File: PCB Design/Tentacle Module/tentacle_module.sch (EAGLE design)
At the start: 58 parts, among them IC1 5.0V, IC3 3.3V, T1 NTD5867NL, T2 NTD5867NL, T3 NTD5867NL, T4 NTD5867NL, U1 OKR-T/10-W12, X3 RJ45-8X, X4 RJ45-8X

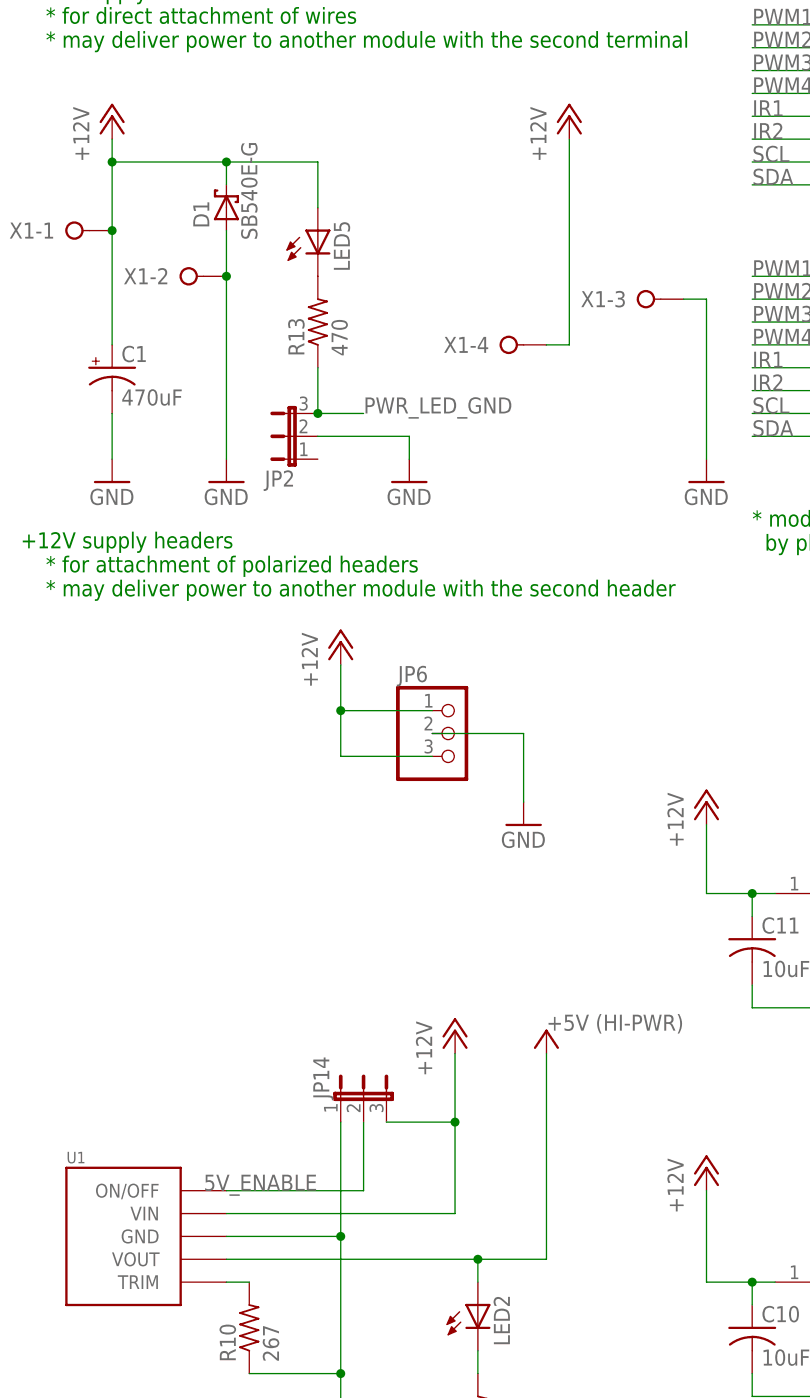
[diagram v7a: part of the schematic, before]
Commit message: Finished updating the Tentacle board
not polished yet though
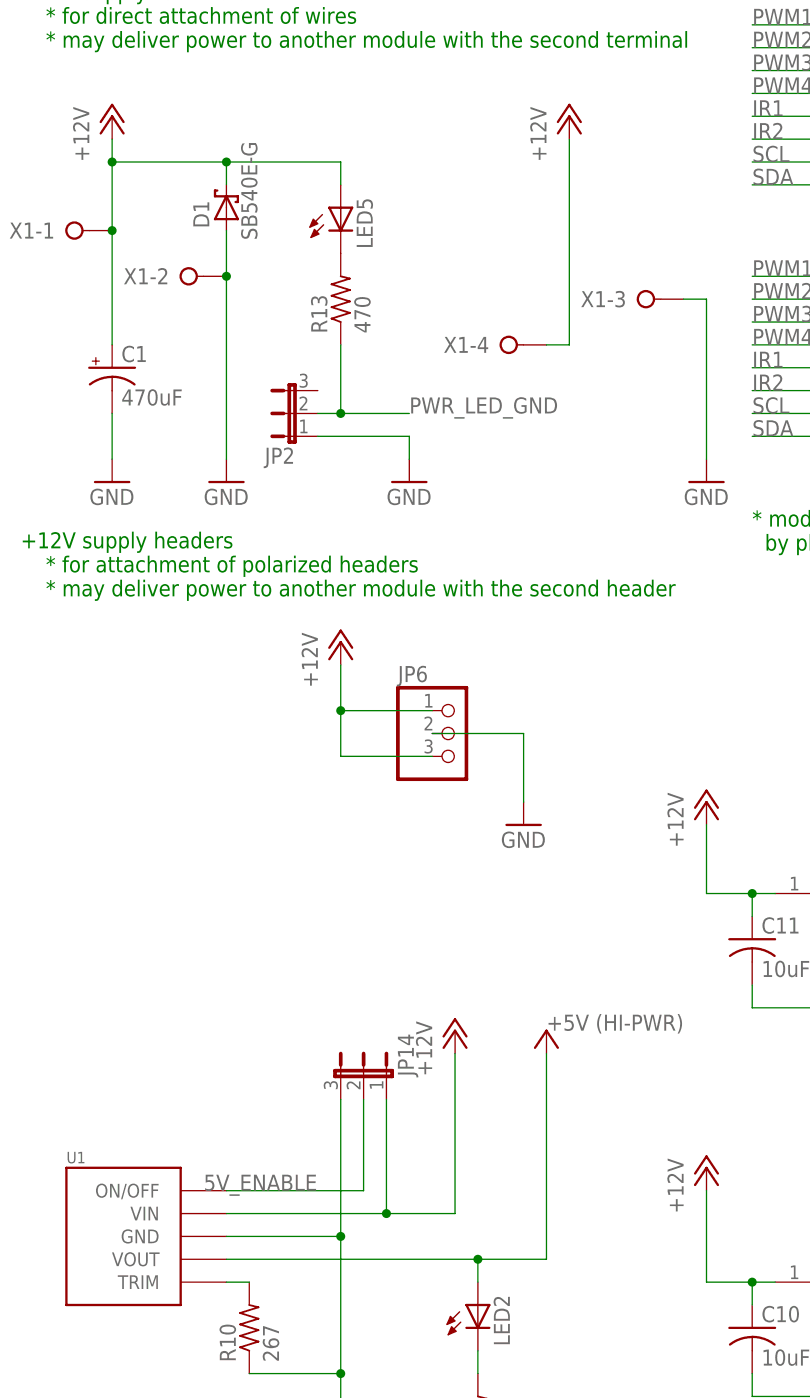
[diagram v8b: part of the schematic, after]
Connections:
- net +12V: now also JP14.1; no longer JP14.3
- net GND: now also JP14.3, JP2.1; no longer JP14.1, JP2.2
- net PWR_LED_GND: now also JP2.2; no longer JP2.3
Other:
- moved on the sheet: JP14, JP2, LED5, R13
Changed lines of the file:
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@@
 <?xml version="1.0" encoding="utf-8"?>
 <!DOCTYPE eagle SYSTEM "eagle.dtd">
-<eagle version="7.0.0">
+<eagle version="7.1.0">
 <drawing>
 <settings>
@@
 <attribute name="VALUE" x="39.751" y="175.006" size="1.778" layer="96" rot="R270"/>
 </instance>
-<instance part="LED5" gate="G$1" x="48.26" y="165.1"/>
-<instance part="R13" gate="G$1" x="48.26" y="154.94" rot="R90"/>
+<instance part="LED5" gate="G$1" x="50.8" y="167.64"/>
+<instance part="R13" gate="G$1" x="50.8" y="157.48" rot="R90"/>
 <instance part="X6" gate="-1" x="226.06" y="109.22"/>
 <instance part="X6" gate="-2" x="226.06" y="104.14"/>
@@
 <instance part="U1" gate="G$1" x="27.94" y="53.34"/>
 <instance part="P+13" gate="1" x="63.5" y="76.2"/>
-<instance part="JP14" gate="1" x="53.34" y="68.58"/>
+<instance part="JP14" gate="1" x="53.34" y="71.12" rot="MR0"/>
 <instance part="PE1" gate="1" x="50.8" y="22.86"/>
 <instance part="P+3" gate="1" x="73.66" y="76.2" smashed="yes">
@@
 <instance part="LED2" gate="G$1" x="66.04" y="45.72"/>
 <instance part="R11" gate="G$1" x="66.04" y="33.02" rot="R90"/>
-<instance part="JP2" gate="1" x="45.72" y="142.24" rot="R90"/>
+<instance part="JP2" gate="1" x="45.72" y="144.78" rot="R90"/>
 <instance part="C3" gate="G$1" x="139.7" y="86.36"/>
 <instance part="C5" gate="G$1" x="139.7" y="43.18"/>
@@
 <pinref part="D1" gate="G$1" pin="C"/>
 <wire x1="38.1" y1="172.72" x2="38.1" y2="170.18" width="0.1524" layer="91"/>
-<wire x1="38.1" y1="172.72" x2="48.26" y2="172.72" width="0.1524" layer="91"/>
+<wire x1="38.1" y1="172.72" x2="50.8" y2="172.72" width="0.1524" layer="91"/>
 <junction x="38.1" y="172.72"/>
 <pinref part="X1" gate="-1" pin="KL"/>
 <junction x="25.4" y="165.1"/>
 <pinref part="LED5" gate="G$1" pin="A"/>
-<wire x1="48.26" y1="172.72" x2="48.26" y2="167.64" width="0.1524" layer="91"/>
+<wire x1="50.8" y1="172.72" x2="50.8" y2="170.18" width="0.1524" layer="91"/>
 </segment>
 <segment>
@@
 <pinref part="U1" gate="G$1" pin="VIN"/>
 <pinref part="P+13" gate="1" pin="+12V"/>
-<wire x1="38.1" y1="55.88" x2="63.5" y2="55.88" width="0.1524" layer="91"/>
-<wire x1="63.5" y1="55.88" x2="63.5" y2="66.04" width="0.1524" layer="91"/>
-<pinref part="JP14" gate="1" pin="3"/>
-<wire x1="63.5" y1="66.04" x2="63.5" y2="73.66" width="0.1524" layer="91"/>
-<wire x1="55.88" y1="66.04" x2="63.5" y2="66.04" width="0.1524" layer="91"/>
-<junction x="63.5" y="66.04"/>
+<wire x1="38.1" y1="55.88" x2="55.88" y2="55.88" width="0.1524" layer="91"/>
+<wire x1="55.88" y1="55.88" x2="63.5" y2="55.88" width="0.1524" layer="91"/>
+<wire x1="63.5" y1="55.88" x2="63.5" y2="73.66" width="0.1524" layer="91"/>
+<pinref part="JP14" gate="1" pin="1"/>
+<wire x1="55.88" y1="68.58" x2="55.88" y2="55.88" width="0.1524" layer="91"/>
+<junction x="55.88" y="55.88"/>
 </segment>
 </net>
@@
 <segment>
 <pinref part="PE1" gate="1" pin="GND"/>
-<pinref part="JP14" gate="1" pin="1"/>
 <pinref part="U1" gate="G$1" pin="GND"/>
 <wire x1="50.8" y1="25.4" x2="50.8" y2="38.1" width="0.1524" layer="91"/>
 <wire x1="50.8" y1="38.1" x2="50.8" y2="53.34" width="0.1524" layer="91"/>
-<wire x1="50.8" y1="53.34" x2="50.8" y2="66.04" width="0.1524" layer="91"/>
 <wire x1="38.1" y1="53.34" x2="50.8" y2="53.34" width="0.1524" layer="91"/>
-<junction x="50.8" y="53.34"/>
 <pinref part="R10" gate="G$1" pin="1"/>
 <wire x1="40.64" y1="38.1" x2="50.8" y2="38.1" width="0.1524" layer="91"/>
 <junction x="50.8" y="38.1"/>
+<pinref part="JP14" gate="1" pin="3"/>
+<wire x1="50.8" y1="53.34" x2="50.8" y2="68.58" width="0.1524" layer="91"/>
+<junction x="50.8" y="53.34"/>
 </segment>
 <segment>
 <pinref part="PE18" gate="1" pin="GND"/>
 <wire x1="58.42" y1="142.24" x2="58.42" y2="139.7" width="0.1524" layer="91"/>
-<pinref part="JP2" gate="1" pin="2"/>
+<pinref part="JP2" gate="1" pin="1"/>
 <wire x1="48.26" y1="142.24" x2="58.42" y2="142.24" width="0.1524" layer="91"/>
 </segment>
@@
 <pinref part="U1" gate="G$1" pin="ON/OFF"/>
 <wire x1="38.1" y1="58.42" x2="53.34" y2="58.42" width="0.1524" layer="91"/>
+<label x="35.56" y="58.42" size="1.778" layer="95"/>
 <pinref part="JP14" gate="1" pin="2"/>
-<wire x1="53.34" y1="58.42" x2="53.34" y2="66.04" width="0.1524" layer="91"/>
-<label x="35.56" y="58.42" size="1.778" layer="95"/>
+<wire x1="53.34" y1="58.42" x2="53.34" y2="68.58" width="0.1524" layer="91"/>
 </segment>
 </net>
@@
 </net>
 <net name="PWR_LED_GND" class="0">
-<segment>
-<pinref part="R13" gate="G$1" pin="1"/>
-<wire x1="48.26" y1="149.86" x2="48.26" y2="144.78" width="0.1524" layer="91"/>
-<pinref part="JP2" gate="1" pin="3"/>
-<label x="53.34" y="144.78" size="1.778" layer="95"/>
-<wire x1="48.26" y1="144.78" x2="53.34" y2="144.78" width="0.1524" layer="91"/>
-<junction x="48.26" y="144.78"/>
-</segment>
 <segment>
 <pinref part="R11" gate="G$1" pin="1"/>
@@
 <label x="73.66" y="25.4" size="1.778" layer="95"/>
 </segment>
-</net>
+<segment>
+<pinref part="JP2" gate="1" pin="2"/>
+<wire x1="48.26" y1="144.78" x2="50.8" y2="144.78" width="0.1524" layer="91"/>
+<wire x1="50.8" y1="144.78" x2="50.8" y2="152.4" width="0.1524" layer="91"/>
+<pinref part="R13" gate="G$1" pin="1"/>
+<label x="58.42" y="144.78" size="1.778" layer="95"/>
+<wire x1="50.8" y1="144.78" x2="58.42" y2="144.78" width="0.1524" layer="91"/>
+<junction x="50.8" y="144.78"/>
+</segment>
+</net>
